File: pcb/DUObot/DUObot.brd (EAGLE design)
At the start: 50 x 70 mm, 22 parts, among them U1 MAX3421ESMD, Y1 16MHZ

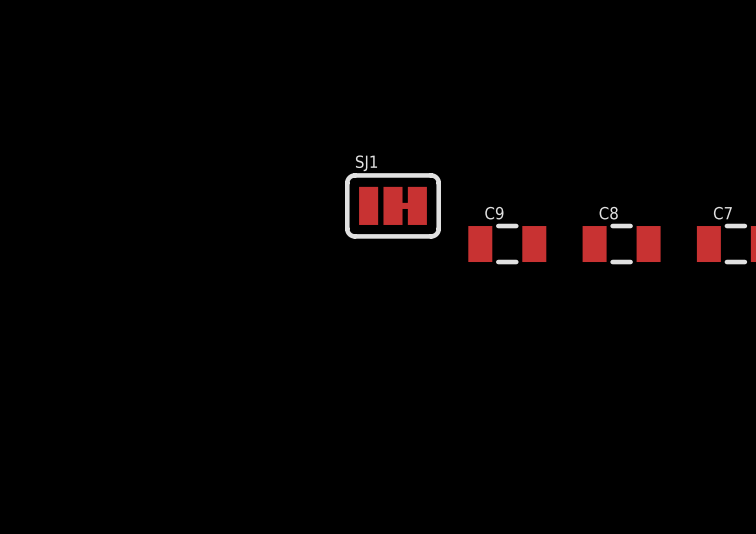
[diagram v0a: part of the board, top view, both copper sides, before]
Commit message: Continue adding components to schematic
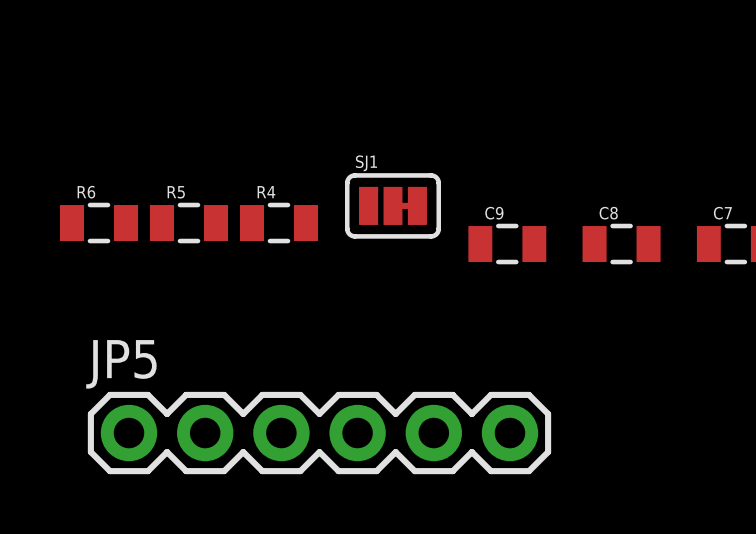
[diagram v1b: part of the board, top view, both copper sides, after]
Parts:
- added JP5: (no value), SparkFun-Connectors:1X06
- added R4, R5: 33, SparkFun-Passives:0805
- added R6: 2.2k, SparkFun-Passives:0805
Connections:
- new net MISO: JP3.1, MCU.22
- new net MOSI: JP3.4, MCU.21
- new net N$10: JP4.D-, R5.1
- new net N$11: R6.1, U1.18
- new net N$7: JP4.D+, R4.1
- new net N$8: R5.2, U1.20
- new net N$9: R4.2, U1.21
- new net RX0: JP5.3, MCU.2
- new net RX1: MCU.45
- new net SCK: JP3.3, MCU.20
- new net SS: MCU.19
- new net TX0: JP5.2, MCU.3
- new net TX1: MCU.46
- net 3.3V: now also R6.2, U1.2, U1.23
- net 5V: now also JP3.2, JP4.VBUS, JP5.4
- net DTR: now also JP5.1
- net GND: now also JP3.6, JP4.GND, JP5.5, JP5.6, U1.19, U1.3
- net LENCA: now also MCU.69
- net LENCB: now also MCU.68
- net LIN1: now also MCU.35
- net LIN2: now also MCU.36
- net LPWM: now also MCU.39
- net RENCA: now also MCU.67
- net RENCB: now also MCU.66
- net RESET: now also JP3.5
- net RIN1: now also MCU.37
- net RIN2: now also MCU.38
- net RPWM: now also MCU.40
- net STBY: now also MCU.41
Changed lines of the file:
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@@
 <attribute name="PROD_ID" value="CONN-09520" x="15" y="59.5" size="1.778" layer="27" rot="R270" display="off"/>
 </element>
+<element name="R4" library="SparkFun-Passives" package="0805" value="33" x="-80" y="-12"/>
+<element name="R5" library="SparkFun-Passives" package="0805" value="33" x="-83" y="-12"/>
+<element name="R6" library="SparkFun-Passives" package="0805" value="2.2k" x="-86" y="-12"/>
+<element name="JP5" library="SparkFun-Connectors" package="1X06" value="" x="-85" y="-19"/>
 </elements>
 <signals>
@@
 <contactref element="Y1" pad="2"/>
 <contactref element="S1" pad="A2"/>
+<contactref element="JP3" pad="6"/>
+<contactref element="U1" pad="3"/>
+<contactref element="U1" pad="19"/>
+<contactref element="JP4" pad="GND"/>
+<contactref element="JP5" pad="6"/>
+<contactref element="JP5" pad="5"/>
+<wire x1="47.585" y1="40.62" x2="40.99" y2="55.22" width="0" layer="19" extent="1-1"/>
 <wire x1="38.796" y1="28.07" x2="47.585" y2="40.62" width="0" layer="19" extent="1-1"/>
 <wire x1="33" y1="28" x2="36.764" y2="28.07" width="0" layer="19" extent="1-1"/>
@@
 <wire x1="17" y1="34.5" x2="17" y2="25.5" width="0" layer="19" extent="1-1"/>
 <wire x1="25.5" y1="39" x2="17" y2="34.5" width="0" layer="19" extent="1-1"/>
+<wire x1="18.72" y1="46.38" x2="25.5" y2="39" width="0" layer="19" extent="1-1"/>
+<wire x1="11.72" y1="47.88" x2="18.72" y2="46.38" width="0" layer="19" extent="1-1"/>
+<wire x1="11.5" y1="55.288" x2="11.72" y2="47.88" width="0" layer="19" extent="1-1"/>
 <wire x1="10.52" y1="3.75" x2="22.85" y2="4.19" width="0" layer="19" extent="1-1"/>
 <wire x1="-37.2" y1="-12.7" x2="10.52" y2="3.75" width="0" layer="19" extent="1-1"/>
@@
 <wire x1="-63.87" y1="-12.7" x2="-60.06" y2="-12.7" width="0" layer="19" extent="1-1"/>
 <wire x1="-67.68" y1="-12.7" x2="-63.87" y2="-12.7" width="0" layer="19" extent="1-1"/>
+<wire x1="-72.3" y1="-19" x2="-67.68" y2="-12.7" width="0" layer="19" extent="1-1"/>
+<wire x1="-74.84" y1="-19" x2="-72.3" y2="-19" width="0" layer="19" extent="1-1"/>
 </signal>
 <signal name="VCC">
@@
 <signal name="LENCA">
 <contactref element="JP1" pad="3"/>
+<contactref element="MCU" pad="69"/>
+<wire x1="35.68" y1="3.75" x2="22" y2="39" width="0" layer="19" extent="1-1"/>
 </signal>
 <signal name="LENCB">
 <contactref element="JP1" pad="2"/>
+<contactref element="MCU" pad="68"/>
+<wire x1="34.68" y1="3.75" x2="22.5" y2="39" width="0" layer="19" extent="1-1"/>
 </signal>
 <signal name="RENCA">
 <contactref element="JP2" pad="3"/>
+<contactref element="MCU" pad="67"/>
+<wire x1="12.52" y1="3.75" x2="23" y2="39" width="0" layer="19" extent="1-1"/>
 </signal>
 <signal name="RENCB">
 <contactref element="JP2" pad="2"/>
+<contactref element="MCU" pad="66"/>
+<wire x1="11.52" y1="3.75" x2="23.5" y2="39" width="0" layer="19" extent="1-1"/>
 </signal>
 <signal name="5V">
@@
 <contactref element="C6" pad="1"/>
 <contactref element="SJ1" pad="3"/>
+<contactref element="JP3" pad="2"/>
+<contactref element="JP4" pad="VBUS"/>
+<contactref element="JP5" pad="4"/>
+<wire x1="-75.3872" y1="-11.43" x2="-77.38" y2="-19" width="0" layer="19" extent="1-1"/>
 <wire x1="-69.48" y1="-12.7" x2="-75.3872" y2="-11.43" width="0" layer="19" extent="1-1"/>
 <wire x1="-65.67" y1="-12.7" x2="-69.48" y2="-12.7" width="0" layer="19" extent="1-1"/>
@@
 <wire x1="26" y1="39" x2="17" y2="35" width="0" layer="19" extent="1-1"/>
 <wire x1="33" y1="27.5" x2="23.5" y2="23" width="0" layer="19" extent="1-1"/>
+<wire x1="18.5" y1="55.288" x2="26" y2="39" width="0" layer="19" extent="1-1"/>
+<wire x1="35.91" y1="55.22" x2="18.5" y2="55.288" width="0" layer="19" extent="1-1"/>
 <wire x1="36.68" y1="3.75" x2="24.355" y2="17.516" width="0" layer="19" extent="1-1"/>
 </signal>
 <signal name="LPWM">
 <contactref element="U$1" pad="23"/>
+<contactref element="MCU" pad="39"/>
+<wire x1="22.405" y1="17.516" x2="33" y2="31.5" width="0" layer="19" extent="1-1"/>
 </signal>
 <signal name="LIN2">
 <contactref element="U$1" pad="22"/>
+<contactref element="MCU" pad="36"/>
+<wire x1="23.055" y1="17.516" x2="33" y2="30" width="0" layer="19" extent="1-1"/>
 </signal>
 <signal name="LIN1">
 <contactref element="U$1" pad="21"/>
+<contactref element="MCU" pad="35"/>
+<wire x1="23.705" y1="17.516" x2="33" y2="29.5" width="0" layer="19" extent="1-1"/>
 </signal>
 <signal name="STBY">
 <contactref element="U$1" pad="19"/>
+<contactref element="MCU" pad="41"/>
+<wire x1="25.005" y1="17.516" x2="33" y2="32.5" width="0" layer="19" extent="1-1"/>
 </signal>
 <signal name="RIN1">
 <contactref element="U$1" pad="17"/>
+<contactref element="MCU" pad="37"/>
+<wire x1="26.305" y1="17.516" x2="33" y2="30.5" width="0" layer="19" extent="1-1"/>
 </signal>
 <signal name="RPWM">
 <contactref element="U$1" pad="15"/>
+<contactref element="MCU" pad="40"/>
+<wire x1="27.605" y1="17.516" x2="33" y2="32" width="0" layer="19" extent="1-1"/>
 </signal>
 <signal name="RIN2">
 <contactref element="U$1" pad="16"/>
+<contactref element="MCU" pad="38"/>
+<wire x1="26.955" y1="17.516" x2="33" y2="31" width="0" layer="19" extent="1-1"/>
 </signal>
 <signal name="AREF">
@@
 <contactref element="C9" pad="2"/>
 <contactref element="S1" pad="B2"/>
+<contactref element="JP3" pad="5"/>
+<wire x1="40.99" y1="50.14" x2="47.585" y2="45.12" width="0" layer="19" extent="1-1"/>
 <wire x1="33" y1="27" x2="47.585" y2="45.12" width="0" layer="19" extent="1-1"/>
 <wire x1="-46.62" y1="-12.7" x2="33" y2="27" width="0" layer="19" extent="1-1"/>
@@
 <signal name="3.3V">
 <contactref element="SJ1" pad="1"/>
+<contactref element="U1" pad="23"/>
+<contactref element="U1" pad="2"/>
+<contactref element="R6" pad="2"/>
+<wire x1="-77.0128" y1="-11.43" x2="-85.1" y2="-12" width="0" layer="19" extent="1-1"/>
+<wire x1="11.72" y1="48.38" x2="-77.0128" y2="-11.43" width="0" layer="19" extent="1-1"/>
+<wire x1="18.72" y1="48.38" x2="11.72" y2="48.38" width="0" layer="19" extent="1-1"/>
 </signal>
 <signal name="DTR">
 <contactref element="C9" pad="1"/>
+<contactref element="JP5" pad="1"/>
+<wire x1="-73.29" y1="-12.7" x2="-85" y2="-19" width="0" layer="19" extent="1-1"/>
 </signal>
 <signal name="N$5">
@@
 <wire x1="33" y1="29" x2="36.764" y2="29.27" width="0" layer="19" extent="1-1"/>
 </signal>
+<signal name="TX1">
+<contactref element="MCU" pad="46"/>
+</signal>
+<signal name="RX1">
+<contactref element="MCU" pad="45"/>
+</signal>
+<signal name="TX0">
+<contactref element="MCU" pad="3"/>
+<contactref element="JP5" pad="2"/>
+<wire x1="20" y1="23" x2="-82.46" y2="-19" width="0" layer="19" extent="1-1"/>
+</signal>
+<signal name="RX0">
+<contactref element="MCU" pad="2"/>
+<contactref element="JP5" pad="3"/>
+<wire x1="19.5" y1="23" x2="-79.92" y2="-19" width="0" layer="19" extent="1-1"/>
+</signal>
+<signal name="MISO">
+<contactref element="MCU" pad="22"/>
+<contactref element="JP3" pad="1"/>
+<wire x1="29.5" y1="23" x2="35.91" y2="50.14" width="0" layer="19" extent="1-1"/>
+</signal>
+<signal name="MOSI">
+<contactref element="MCU" pad="21"/>
+<contactref element="JP3" pad="4"/>
+<wire x1="29" y1="23" x2="38.45" y2="55.22" width="0" layer="19" extent="1-1"/>
+</signal>
+<signal name="SCK">
+<contactref element="MCU" pad="20"/>
+<contactref element="JP3" pad="3"/>
+<wire x1="28.5" y1="23" x2="38.45" y2="50.14" width="0" layer="19" extent="1-1"/>
+</signal>
+<signal name="N$8">
+<contactref element="R5" pad="2"/>
+<contactref element="U1" pad="20"/>
+<wire x1="18.72" y1="46.88" x2="-82.1" y2="-12" width="0" layer="19" extent="1-1"/>
+</signal>
+<signal name="N$9">
+<contactref element="U1" pad="21"/>
+<contactref element="R4" pad="2"/>
+<wire x1="18.72" y1="47.38" x2="-79.1" y2="-12" width="0" layer="19" extent="1-1"/>
+</signal>
+<signal name="N$7">
+<contactref element="JP4" pad="D+"/>
+<contactref element="R4" pad="1"/>
+<wire x1="14" y1="55.288" x2="-80.9" y2="-12" width="0" layer="19" extent="1-1"/>
+</signal>
+<signal name="N$10">
+<contactref element="JP4" pad="D-"/>
+<contactref element="R5" pad="1"/>
+<wire x1="16" y1="55.288" x2="-83.9" y2="-12" width="0" layer="19" extent="1-1"/>
+</signal>
+<signal name="N$11">
+<contactref element="R6" pad="1"/>
+<contactref element="U1" pad="18"/>
+<wire x1="18.72" y1="45.88" x2="-86.9" y2="-12" width="0" layer="19" extent="1-1"/>
+</signal>
+<signal name="SS">
+<contactref element="MCU" pad="19"/>
+</signal>
 </signals>

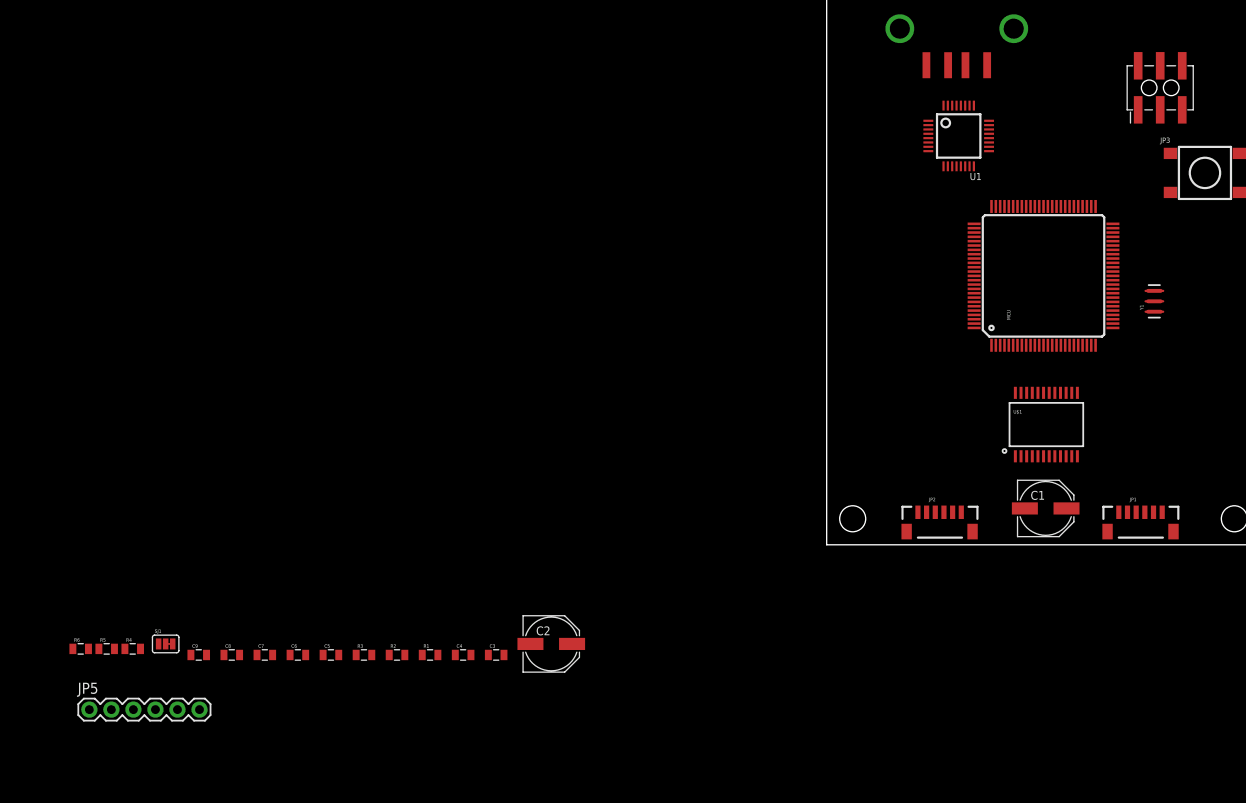
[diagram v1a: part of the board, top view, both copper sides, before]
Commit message: Working on power select control circuitry
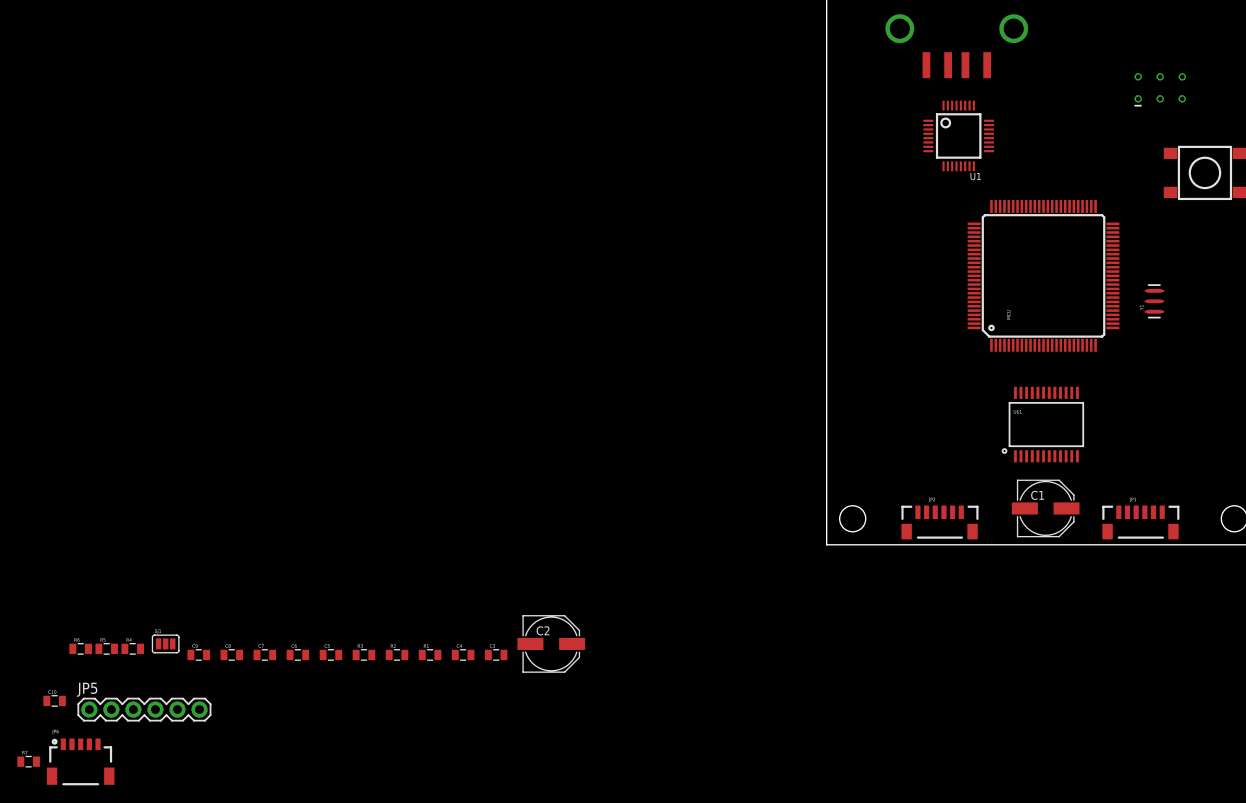
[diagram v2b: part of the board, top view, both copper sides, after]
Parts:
- added C10: 0.1u, SparkFun-Passives:0805
- added JP6: (no value), SparkFun-Connectors:1X05-1MM-RA
- added R7: 1M, SparkFun-Passives:0805
- JP3: value (none) -> AVR_SPI_PRG_6TESTPOINTS; device SparkFun-Connectors:2X3_SMT_POSTS -> SparkFun-Connectors:2X3_TEST_POINTS
- SJ1: value (none) -> JUMPER-PAD-3-NOYES_SILK; device SparkFun-Passives:PAD-JUMPER-3-2OF3_NC_BY_TRACE_YES_SILK_FULL_BOX -> SparkFun-Passives:PAD-JUMPER-3-NO_YES_SILK
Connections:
- net 3.3V: now also JP6.2
- net 5V: now also C10.1, JP6.1
- net GND: now also C10.2, JP6.3, S1.B2; no longer S1.A2
- net N$5: now also R7.2
- net N$6: now also R7.1
- net RESET: now also S1.A2; no longer S1.B2
- net SCL: now also JP6.5
- net SDA: now also JP6.4
